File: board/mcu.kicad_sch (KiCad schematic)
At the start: 10 parts, among them J10 Conn_01x03_Male, J16 Conn_01x02_Male, U1 STM32L476RGT6

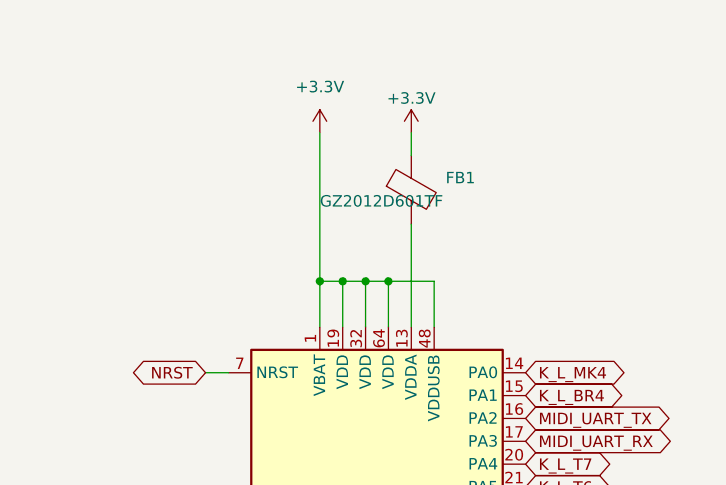
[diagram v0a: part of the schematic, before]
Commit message: created firmware project. Tested MIDI communication over MIDI port as well as USB MIDI
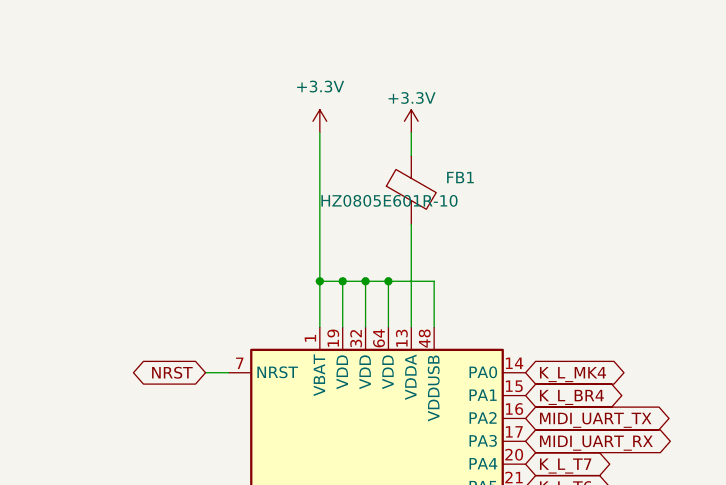
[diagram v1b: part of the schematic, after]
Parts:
- C16: Digi-Key Part Number (none) -> 1276-1003-1-ND
- C2, C3: Digi-Key Part Number (none) -> 1276-1829-1-ND
- FB1: value GZ2012D601TF -> HZ0805E601R-10; Digi-Key Part Number (none) -> 240-2399-1-ND; LCSC C1017 -> (none); MANUFACTURER Sunlord -> Laird-Signal Integrity Products; Manufacturer_Name Sunlord -> Laird-Signal Integrity Products; Manufacturer_Part_Number GZ2012D601TF -> HZ0805E601R-10
- J10: Digi-Key Part Number (none) -> HTSW-103-14-TM-S-ND
- J16: Digi-Key Part Number (none) -> HTSW-102-14-TM-S-ND
- R18, R19: Digi-Key Part Number (none) -> P10KDACT-ND; LCSC C17414 -> (none); MANUFACTURER UNI-ROYAL(Uniroyal Elec) -> Panasonic Electronic Components; Manufacturer_Name UNI-ROYAL(Uniroyal Elec) -> Panasonic Electronic Components; Manufacturer_Part_Number 0805W8F1002T5E -> ERA-6AEB103V
- U1: Farnell Part Number (none) -> 2494460
- e1: Digi-Key Part Number (none) -> 887-2014-ND
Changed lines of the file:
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@@
+      (effects (font (size 1.27 1.27)) hide)
+    )
+    (property "Digi-Key Part Number" "887-2014-ND" (id 9) (at 125.73 101.6 0)
       (effects (font (size 1.27 1.27)) hide)
     )
@@
     )
     (property "LCSC" "C1798" (id 8) (at 133.35 109.22 0)
+      (effects (font (size 1.27 1.27)) hide)
+    )
+    (property "Digi-Key Part Number" "1276-1829-1-ND" (id 9) (at 133.35 109.22 0)
       (effects (font (size 1.27 1.27)) hide)
     )
@@
       (effects (font (size 1.27 1.27)) hide)
     )
-    (property "Datasheet" "https://datasheet.lcsc.com/lcsc/2206010216_UNI-ROYAL-Uniroyal-Elec-0805W8F1002T5E_C17414.pdf" (id 3) (at 67.31 82.55 0)
+    (property "Datasheet" "" (id 3) (at 67.31 82.55 0)
       (effects (font (size 1.27 1.27)) hide)
     )
@@
       (effects (font (size 1.27 1.27)) hide)
     )
-    (property "MANUFACTURER" "UNI-ROYAL(Uniroyal Elec)" (id 5) (at 67.31 82.55 0)
-      (effects (font (size 1.27 1.27)) hide)
-    )
-    (property "Manufacturer_Name" "UNI-ROYAL(Uniroyal Elec)" (id 6) (at 67.31 82.55 0)
-      (effects (font (size 1.27 1.27)) hide)
-    )
-    (property "Manufacturer_Part_Number" "0805W8F1002T5E" (id 7) (at 67.31 82.55 0)
-      (effects (font (size 1.27 1.27)) hide)
-    )
-    (property "LCSC" "C17414" (id 8) (at 67.31 82.55 0)
+    (property "MANUFACTURER" "Panasonic Electronic Components" (id 5) (at 67.31 82.55 0)
+      (effects (font (size 1.27 1.27)) hide)
+    )
+    (property "Manufacturer_Name" "Panasonic Electronic Components" (id 6) (at 67.31 82.55 0)
+      (effects (font (size 1.27 1.27)) hide)
+    )
+    (property "Manufacturer_Part_Number" "ERA-6AEB103V" (id 7) (at 67.31 82.55 0)
+      (effects (font (size 1.27 1.27)) hide)
+    )
+    (property "LCSC" "" (id 8) (at 67.31 82.55 0)
+      (effects (font (size 1.27 1.27)) hide)
+    )
+    (property "Digi-Key Part Number" "P10KDACT-ND" (id 9) (at 67.31 82.55 0)
       (effects (font (size 1.27 1.27)) hide)
     )
@@
     )
     (property "Manufacturer_Part_Number" "STM32L476RGT6" (id 8) (at 189.23 102.87 0)
+      (effects (font (size 1.27 1.27)) hide)
+    )
+    (property "Farnell Part Number" "2494460" (id 9) (at 189.23 102.87 0)
       (effects (font (size 1.27 1.27)) hide)
     )
@@
       (effects (font (size 1.27 1.27)) hide)
     )
+    (property "Digi-Key Part Number" "HTSW-103-14-TM-S-ND" (id 8) (at 55.88 91.44 0)
+      (effects (font (size 1.27 1.27)) hide)
+    )
     (pin "1")
     (pin "2")
@@
       (effects (font (size 1.27 1.27)) hide)
     )
+    (property "Digi-Key Part Number" "1276-1003-1-ND" (id 9) (at 74.93 35.56 0)
+      (effects (font (size 1.27 1.27)) hide)
+    )
     (pin "1")
     (pin "2")
@@
       (effects (font (size 1.27 1.27)) (justify left))
     )
-    (property "Value" "GZ2012D601TF" (id 1) (at 181.61 43.18 0)
+    (property "Value" "HZ0805E601R-10" (id 1) (at 181.61 43.18 0)
       (effects (font (size 1.27 1.27)) (justify left))
     )
@@
       (effects (font (size 1.27 1.27)) hide)
     )
-    (property "Datasheet" "https://datasheet.lcsc.com/lcsc/2109181830_Sunlord-GZ2012D601TF_C1017.pdf" (id 3) (at 191.77 41.91 0)
-      (effects (font (size 1.27 1.27)) hide)
-    )
-    (property "Description" "500mA 1 300mΩ 600Ω@100MHz ±25% 0805 Ferrite Beads ROHS" (id 4) (at 191.77 41.91 0)
-      (effects (font (size 1.27 1.27)) hide)
-    )
-    (property "MANUFACTURER" "Sunlord" (id 5) (at 191.77 41.91 0)
-      (effects (font (size 1.27 1.27)) hide)
-    )
-    (property "Manufacturer_Name" "Sunlord" (id 6) (at 191.77 41.91 0)
-      (effects (font (size 1.27 1.27)) hide)
-    )
-    (property "Manufacturer_Part_Number" "GZ2012D601TF" (id 7) (at 191.77 41.91 0)
-      (effects (font (size 1.27 1.27)) hide)
-    )
-    (property "LCSC" "C1017" (id 8) (at 191.77 41.91 0)
+    (property "Datasheet" "https://media.digikey.com/pdf/Data%20Sheets/Laird%20Technologies/EMI_Filtering_and_RF_Inductors.pdf" (id 3) (at 191.77 41.91 0)
+      (effects (font (size 1.27 1.27)) hide)
+    )
+    (property "Description" "600 Ohms @ 100 MHz 1 Power, Signal Line Ferrite Bead 0805 (2012 Metric) 500mA 300mOhm" (id 4) (at 191.77 41.91 0)
+      (effects (font (size 1.27 1.27)) hide)
+    )
+    (property "MANUFACTURER" "Laird-Signal Integrity Products" (id 5) (at 191.77 41.91 0)
+      (effects (font (size 1.27 1.27)) hide)
+    )
+    (property "Manufacturer_Name" "Laird-Signal Integrity Products" (id 6) (at 191.77 41.91 0)
+      (effects (font (size 1.27 1.27)) hide)
+    )
+    (property "Manufacturer_Part_Number" "HZ0805E601R-10" (id 7) (at 191.77 41.91 0)
+      (effects (font (size 1.27 1.27)) hide)
+    )
+    (property "LCSC" "" (id 8) (at 191.77 41.91 0)
+      (effects (font (size 1.27 1.27)) hide)
+    )
+    (property "Digi-Key Part Number" "240-2399-1-ND" (id 9) (at 191.77 41.91 0)
       (effects (font (size 1.27 1.27)) hide)
     )
@@
       (effects (font (size 1.27 1.27)) hide)
     )
-    (property "Datasheet" "https://datasheet.lcsc.com/lcsc/2206010216_UNI-ROYAL-Uniroyal-Elec-0805W8F1002T5E_C17414.pdf" (id 3) (at 67.31 99.06 0)
+    (property "Datasheet" "" (id 3) (at 67.31 99.06 0)
       (effects (font (size 1.27 1.27)) hide)
     )
@@
       (effects (font (size 1.27 1.27)) hide)
     )
-    (property "MANUFACTURER" "UNI-ROYAL(Uniroyal Elec)" (id 5) (at 67.31 99.06 0)
-      (effects (font (size 1.27 1.27)) hide)
-    )
-    (property "Manufacturer_Name" "UNI-ROYAL(Uniroyal Elec)" (id 6) (at 67.31 99.06 0)
-      (effects (font (size 1.27 1.27)) hide)
-    )
-    (property "Manufacturer_Part_Number" "0805W8F1002T5E" (id 7) (at 67.31 99.06 0)
-      (effects (font (size 1.27 1.27)) hide)
-    )
-    (property "LCSC" "C17414" (id 8) (at 67.31 99.06 0)
+    (property "MANUFACTURER" "Panasonic Electronic Components" (id 5) (at 67.31 99.06 0)
+      (effects (font (size 1.27 1.27)) hide)
+    )
+    (property "Manufacturer_Name" "Panasonic Electronic Components" (id 6) (at 67.31 99.06 0)
+      (effects (font (size 1.27 1.27)) hide)
+    )
+    (property "Manufacturer_Part_Number" "ERA-6AEB103V" (id 7) (at 67.31 99.06 0)
+      (effects (font (size 1.27 1.27)) hide)
+    )
+    (property "LCSC" "" (id 8) (at 67.31 99.06 0)
+      (effects (font (size 1.27 1.27)) hide)
+    )
+    (property "Digi-Key Part Number" "P10KDACT-ND" (id 9) (at 67.31 99.06 0)
       (effects (font (size 1.27 1.27)) hide)
     )
@@
     )
     (property "LCSC" "C1798" (id 8) (at 118.11 109.22 0)
+      (effects (font (size 1.27 1.27)) hide)
+    )
+    (property "Digi-Key Part Number" "1276-1829-1-ND" (id 9) (at 118.11 109.22 0)
       (effects (font (size 1.27 1.27)) hide)
     )
@@
       (effects (font (size 1.27 1.27)) hide)
     )
+    (property "Digi-Key Part Number" "HTSW-102-14-TM-S-ND" (id 8) (at 48.26 33.02 0)
+      (effects (font (size 1.27 1.27)) hide)
+    )
